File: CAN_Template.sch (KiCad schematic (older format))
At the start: 21 parts, among them U6 SN74LVC1T45DBVR, U7 SN65HVD1050D, U8 MCP2515-xSO, U9 SN74LVC1T45DBVR

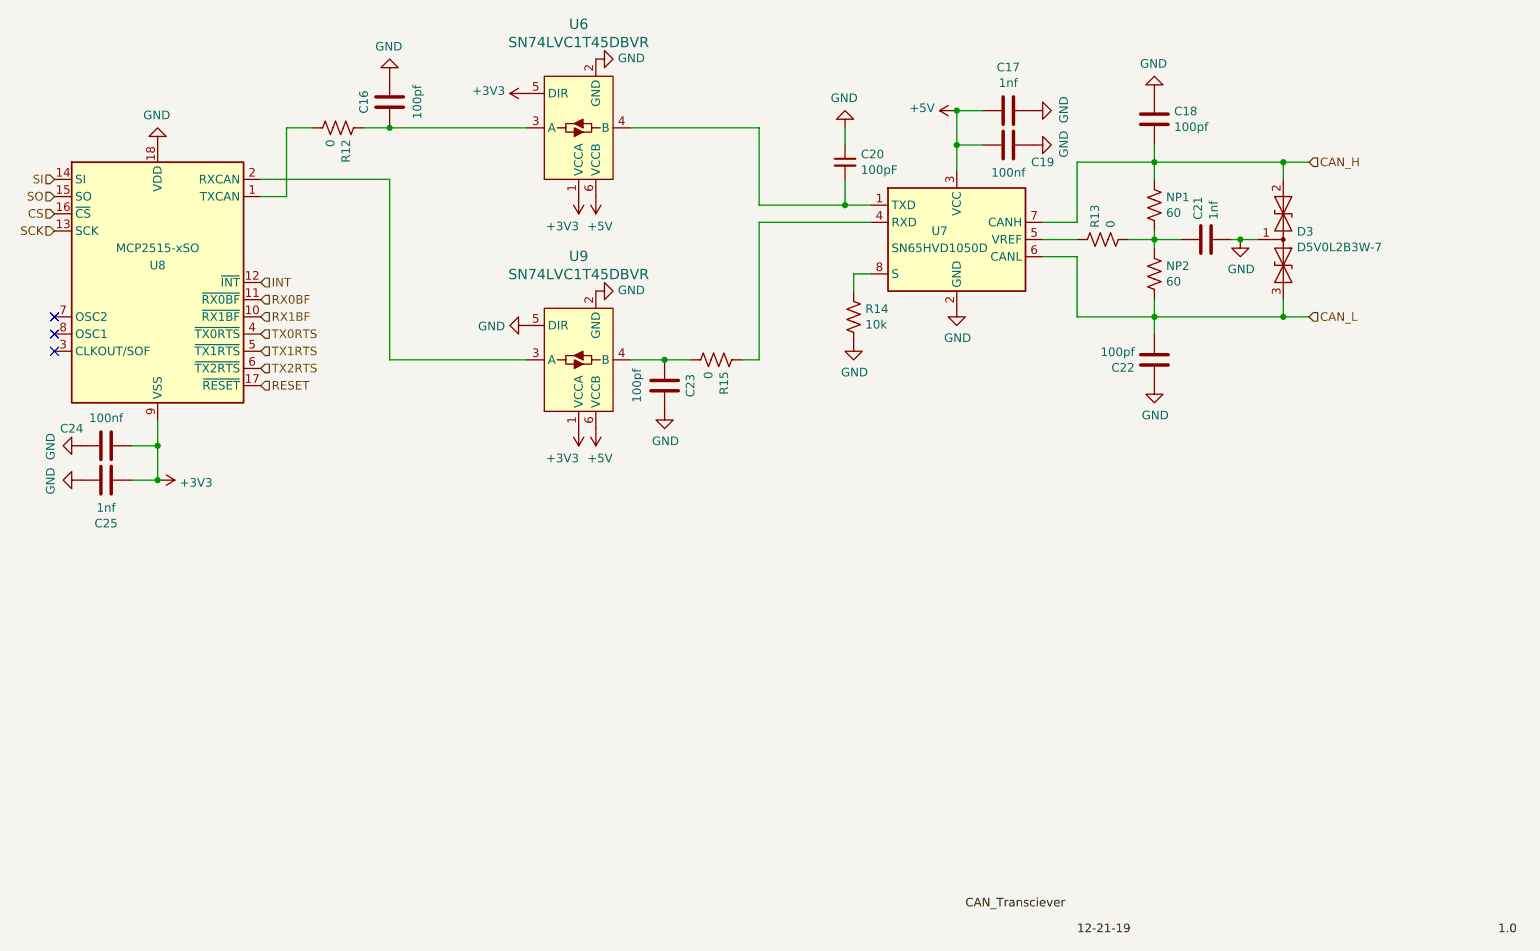
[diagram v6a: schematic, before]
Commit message: Added caps to xbee input, header to SWD pins
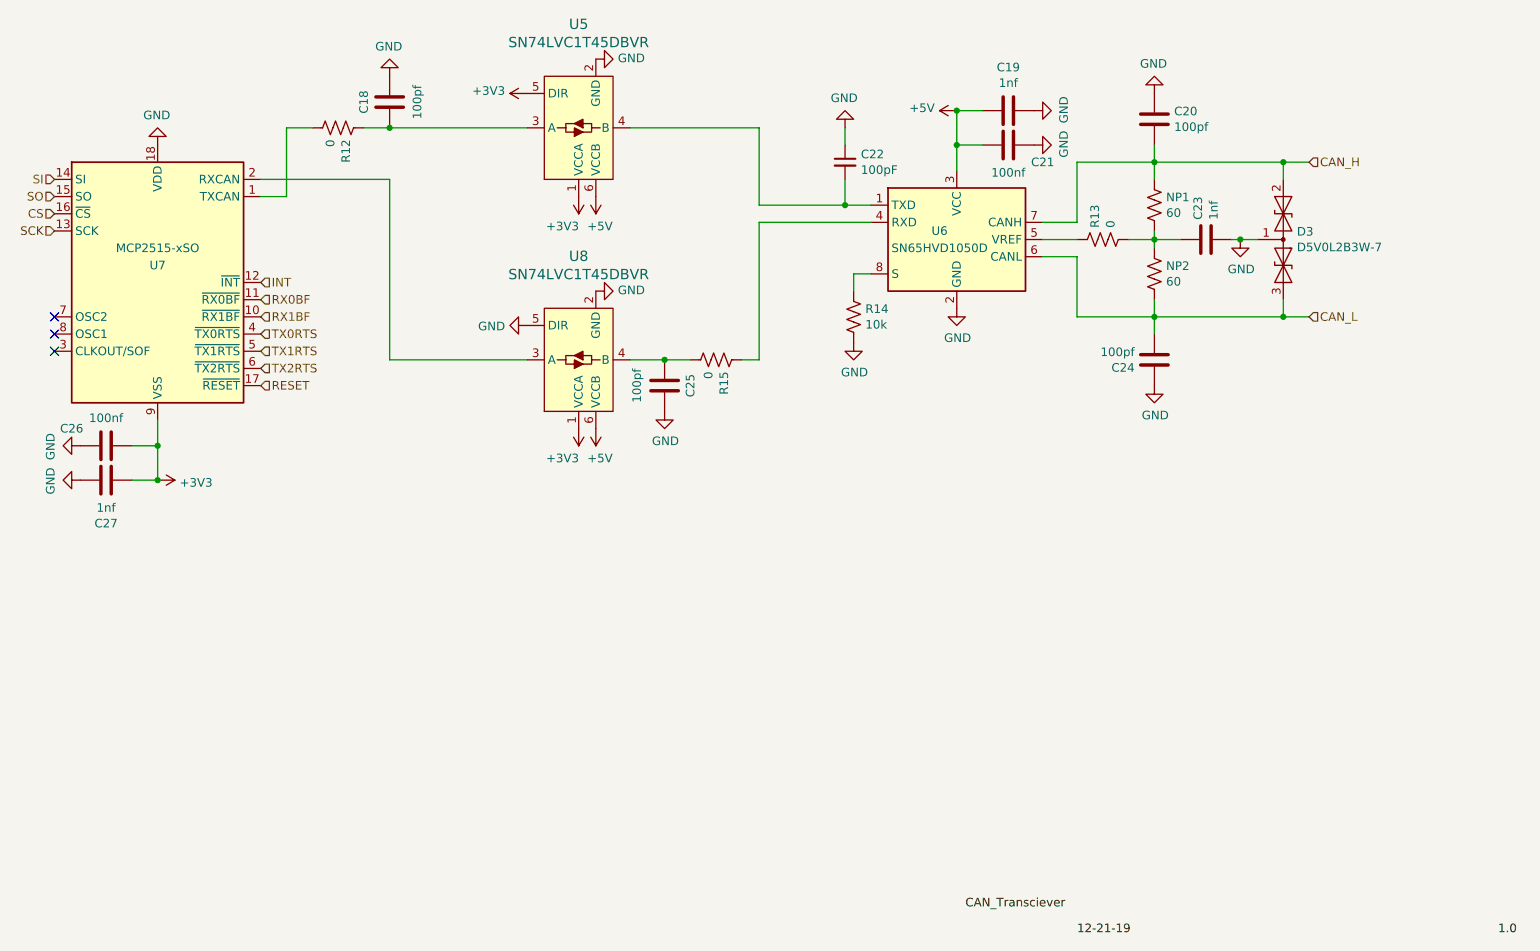
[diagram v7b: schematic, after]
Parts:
- renumbered C16 to C18, C17 to C19, C18 to C20, C19 to C21, C20 to C22, C21 to C23, C22 to C24, C23 to C25, C24 to C26, C25 to C27, U6 to U5, U7 to U6, U8 to U7, U9 to U8
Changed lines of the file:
@@
 $EndComp
 $Comp
-L Device:C C17
+L Device:C C19
 U 1 1 5DCB9CD1
 P 7750 2850
-F 0 "C17" V 7498 2850 50  0000 C CNN
+F 0 "C19" V 7498 2850 50  0000 C CNN
 F 1 "1nf" V 7589 2850 50  0000 C CNN
 F 2 "Capacitor_SMD:C_0805_2012Metric" H 7788 2700 50  0001 C CNN
@@
 $EndComp
 $Comp
-L Device:C C19
+L Device:C C21
 U 1 1 5DCBAD85
 P 7750 3050
-F 0 "C19" V 7650 2850 50  0000 C CNN
+F 0 "C21" V 7650 2850 50  0000 C CNN
 F 1 "100nf" V 7589 3050 50  0000 C CNN
 F 2 "Capacitor_SMD:C_0805_2012Metric" H 7788 2900 50  0001 C CNN
@@
 $EndComp
 $Comp
-L power:GND #PWR055
+L power:GND #PWR057
 U 1 1 5DCE500D
 P 2800 3050
-F 0 "#PWR055" H 2800 2800 50  0001 C CNN
+F 0 "#PWR057" H 2800 2800 50  0001 C CNN
 F 1 "GND" H 2805 2877 50  0000 C CNN
 F 2 "" H 2800 3050 50  0001 C CNN
@@
 $EndComp
 $Comp
-L Device:C C22
+L Device:C C24
 U 1 1 5DCE6703
 P 8600 4300
-F 0 "C22" H 8715 4346 50  0000 L CNN
+F 0 "C24" H 8715 4346 50  0000 L CNN
 F 1 "100pf" H 8715 4255 50  0000 L CNN
 F 2 "Capacitor_SMD:C_0805_2012Metric" H 8638 4150 50  0001 C CNN
@@
 $EndComp
 $Comp
-L Device:C C21
+L Device:C C23
 U 1 1 5DCEFDFD
 P 8900 3600
-F 0 "C21" H 9015 3646 50  0000 L CNN
+F 0 "C23" H 9015 3646 50  0000 L CNN
 F 1 "1nf" H 9015 3555 50  0000 L CNN
 F 2 "Capacitor_SMD:C_0805_2012Metric" H 8938 3450 50  0001 C CNN
@@
 $EndComp
 $Comp
-L power:GND #PWR064
+L power:GND #PWR066
 U 1 1 5DCF0F65
 P 8600 4450
-F 0 "#PWR064" H 8600 4200 50  0001 C CNN
+F 0 "#PWR066" H 8600 4200 50  0001 C CNN
 F 1 "GND" H 8605 4277 50  0000 C CNN
 F 2 "" H 8600 4450 50  0001 C CNN
@@
 $EndComp
 $Comp
-L power:GND #PWR051
+L power:GND #PWR053
 U 1 1 5DCF11EA
 P 8600 2750
-F 0 "#PWR051" H 8600 2500 50  0001 C CNN
+F 0 "#PWR053" H 8600 2500 50  0001 C CNN
 F 1 "GND" H 8605 2577 50  0000 C CNN
 F 2 "" H 8600 2750 50  0001 C CNN
@@
 $EndComp
 $Comp
-L Interface_CAN_LIN:MCP2515-xSO U8
+L Interface_CAN_LIN:MCP2515-xSO U7
 U 1 1 5DCB05B0
 P 2800 3850
-F 0 "U8" H 2800 3950 50  0000 C CNN
+F 0 "U7" H 2800 3950 50  0000 C CNN
 F 1 "MCP2515-xSO" H 2800 4050 50  0000 C CNN
 F 2 "Package_SO:SOIC-18W_7.5x11.6mm_P1.27mm" H 2800 2950 50  0001 C CIN
@@
 CAN_H
 $Comp
-L Device:C C18
+L Device:C C20
 U 1 1 5DCE5998
 P 8600 2900
-F 0 "C18" H 8715 2946 50  0000 L CNN
+F 0 "C20" H 8715 2946 50  0000 L CNN
 F 1 "100pf" H 8715 2855 50  0000 L CNN
 F 2 "Capacitor_SMD:C_0805_2012Metric" H 8638 2750 50  0001 C CNN
@@
 $EndComp
 $Comp
-L Interface_CAN_LIN:SN65HVD1050D U7
+L Interface_CAN_LIN:SN65HVD1050D U6
 U 1 1 5DD4ABBA
 P 7450 3600
-F 0 "U7" H 7350 3650 50  0000 C CNN
+F 0 "U6" H 7350 3650 50  0000 C CNN
 F 1 "SN65HVD1050D" H 7350 3550 50  0000 C CNN
 F 2 "Package_SO:SOIC-8_3.9x4.9mm_P1.27mm" H 7450 3100 50  0001 C CNN
@@
 Connection ~ 9350 3150
 $Comp
-L power:GND #PWR061
+L power:GND #PWR063
 U 1 1 5E09CBC9
 P 7450 4000
-F 0 "#PWR061" H 7450 3750 50  0001 C CNN
+F 0 "#PWR063" H 7450 3750 50  0001 C CNN
 F 1 "GND" H 7455 3827 50  0000 C CNN
 F 2 "" H 7450 4000 50  0001 C CNN
@@
 $EndComp
 $Comp
-L power:GND #PWR056
+L power:GND #PWR058
 U 1 1 5E0A1057
 P 7900 3050
-F 0 "#PWR056" H 7900 2800 50  0001 C CNN
+F 0 "#PWR058" H 7900 2800 50  0001 C CNN
 F 1 "GND" H 7905 2877 50  0000 C CNN
 F 2 "" H 7900 3050 50  0001 C CNN
@@
 $EndComp
 $Comp
-L power:GND #PWR053
+L power:GND #PWR055
 U 1 1 5E0A1679
 P 7900 2850
-F 0 "#PWR053" H 7900 2600 50  0001 C CNN
+F 0 "#PWR055" H 7900 2600 50  0001 C CNN
 F 1 "GND" H 7905 2677 50  0000 C CNN
 F 2 "" H 7900 2850 50  0001 C CNN
@@
 Connection ~ 7450 3050
 $Comp
-L power:+5V #PWR052
+L power:+5V #PWR054
 U 1 1 5E0A2EDD
 P 7450 2850
-F 0 "#PWR052" H 7450 2700 50  0001 C CNN
+F 0 "#PWR054" H 7450 2700 50  0001 C CNN
 F 1 "+5V" V 7465 2978 50  0000 L CNN
 F 2 "" H 7450 2850 50  0001 C CNN
@@
 	6850 3800 6950 3800
 $Comp
-L power:GND #PWR063
+L power:GND #PWR065
 U 1 1 5E0A7026
 P 6850 4200
-F 0 "#PWR063" H 6850 3950 50  0001 C CNN
+F 0 "#PWR065" H 6850 3950 50  0001 C CNN
 F 1 "GND" H 6855 4027 50  0000 C CNN
 F 2 "" H 6850 4200 50  0001 C CNN
@@
 $EndComp
 $Comp
-L Device:C C25
+L Device:C C27
 U 1 1 5E0BDAE5
 P 2500 5000
-F 0 "C25" V 2248 5000 50  0000 C CNN
+F 0 "C27" V 2248 5000 50  0000 C CNN
 F 1 "1nf" V 2339 5000 50  0000 C CNN
 F 2 "Capacitor_SMD:C_0805_2012Metric" H 2538 4850 50  0001 C CNN
@@
 $EndComp
 $Comp
-L Device:C C24
+L Device:C C26
 U 1 1 5E0BDAEB
 P 2500 4800
-F 0 "C24" V 2400 4600 50  0000 C CNN
+F 0 "C26" V 2400 4600 50  0000 C CNN
 F 1 "100nf" V 2339 4800 50  0000 C CNN
 F 2 "Capacitor_SMD:C_0805_2012Metric" H 2538 4650 50  0001 C CNN
@@
 $EndComp
 $Comp
-L power:GND #PWR068
+L power:GND #PWR070
 U 1 1 5E0BDAF1
 P 2350 4800
-F 0 "#PWR068" H 2350 4550 50  0001 C CNN
+F 0 "#PWR070" H 2350 4550 50  0001 C CNN
 F 1 "GND" H 2355 4627 50  0000 C CNN
 F 2 "" H 2350 4800 50  0001 C CNN
@@
 $EndComp
 $Comp
-L power:GND #PWR069
+L power:GND #PWR071
 U 1 1 5E0BDAF7
 P 2350 5000
-F 0 "#PWR069" H 2350 4750 50  0001 C CNN
+F 0 "#PWR071" H 2350 4750 50  0001 C CNN
 F 1 "GND" H 2355 4827 50  0000 C CNN
 F 2 "" H 2350 5000 50  0001 C CNN
@@
 Connection ~ 2800 4800
 $Comp
-L Device:C C16
+L Device:C C18
 U 1 1 5E0C191D
 P 4150 2800
-F 0 "C16" V 4300 2800 50  0000 C CNN
+F 0 "C18" V 4300 2800 50  0000 C CNN
 F 1 "100pf" V 3989 2800 50  0000 C CNN
 F 2 "Capacitor_SMD:C_0805_2012Metric" H 4188 2650 50  0001 C CNN
@@
 	9050 3600 9100 3600
 $Comp
-L power:GND #PWR059
+L power:GND #PWR061
 U 1 1 5E0C862A
 P 9100 3600
-F 0 "#PWR059" H 9100 3350 50  0001 C CNN
+F 0 "#PWR061" H 9100 3350 50  0001 C CNN
 F 1 "GND" H 9105 3427 50  0000 C CNN
 F 2 "" H 9100 3600 50  0001 C CNN
@@
 CAN_Transciever
 $Comp
-L Device:C_Small C20
+L Device:C_Small C22
 U 1 1 5E22EBAC
 P 6800 3150
-F 0 "C20" H 6892 3196 50  0000 L CNN
+F 0 "C22" H 6892 3196 50  0000 L CNN
 F 1 "100pF" H 6892 3105 50  0000 L CNN
 F 2 "Capacitor_SMD:C_0805_2012Metric" H 6800 3150 50  0001 C CNN
@@
 	6800 3400 6800 3250
 $Comp
-L power:GND #PWR054
+L power:GND #PWR056
 U 1 1 5E231658
 P 6800 2950
-F 0 "#PWR054" H 6800 2700 50  0001 C CNN
+F 0 "#PWR056" H 6800 2700 50  0001 C CNN
 F 1 "GND" H 6805 2777 50  0000 C CNN
 F 2 "" H 6800 2950 50  0001 C CNN
@@
 	6800 3050 6800 2950
 $Comp
-L dk_Logic-Translators-Level-Shifters:SN74LVC1T45DBVR U6
+L dk_Logic-Translators-Level-Shifters:SN74LVC1T45DBVR U5
 U 1 1 5E23BA35
 P 5250 2950
-F 0 "U6" H 5250 2347 60  0000 C CNN
+F 0 "U5" H 5250 2347 60  0000 C CNN
 F 1 "SN74LVC1T45DBVR" H 5250 2453 60  0000 C CNN
 F 2 "digikey-footprints:SOT-23-6" H 5450 3150 60  0001 L CNN
@@
 $EndComp
 $Comp
-L dk_Logic-Translators-Level-Shifters:SN74LVC1T45DBVR U9
+L dk_Logic-Translators-Level-Shifters:SN74LVC1T45DBVR U8
 U 1 1 5E2400EF
 P 5250 4300
-F 0 "U9" H 5250 3697 60  0000 C CNN
+F 0 "U8" H 5250 3697 60  0000 C CNN
 F 1 "SN74LVC1T45DBVR" H 5250 3803 60  0000 C CNN
 F 2 "digikey-footprints:SOT-23-6" H 5450 4500 60  0001 L CNN
@@
 	6300 2950 6300 3400
 $Comp
-L power:GND #PWR062
+L power:GND #PWR064
 U 1 1 5E25071C
 P 4950 4100
-F 0 "#PWR062" H 4950 3850 50  0001 C CNN
+F 0 "#PWR064" H 4950 3850 50  0001 C CNN
 F 1 "GND" V 4955 3972 50  0000 R CNN
 F 2 "" H 4950 4100 50  0001 C CNN
@@
 $EndComp
 $Comp
-L power:GND #PWR048
+L power:GND #PWR050
 U 1 1 5E250D83
 P 5350 2550
-F 0 "#PWR048" H 5350 2300 50  0001 C CNN
+F 0 "#PWR050" H 5350 2300 50  0001 C CNN
 F 1 "GND" V 5355 2422 50  0000 R CNN
 F 2 "" H 5350 2550 50  0001 C CNN
@@
 $EndComp
 $Comp
-L power:GND #PWR060
+L power:GND #PWR062
 U 1 1 5E2516EF
 P 5350 3900
-F 0 "#PWR060" H 5350 3650 50  0001 C CNN
+F 0 "#PWR062" H 5350 3650 50  0001 C CNN
 F 1 "GND" V 5355 3772 50  0000 R CNN
 F 2 "" H 5350 3900 50  0001 C CNN
@@
 Connection ~ 6800 3400
 $Comp
-L power:+3V3 #PWR050
+L power:+3V3 #PWR052
 U 1 1 5E2603B1
 P 4950 2750
-F 0 "#PWR050" H 4950 2600 50  0001 C CNN
+F 0 "#PWR052" H 4950 2600 50  0001 C CNN
 F 1 "+3V3" V 4965 2878 50  0000 L CNN
 F 2 "" H 4950 2750 50  0001 C CNN
@@
 	6300 3500 6300 4300
 $Comp
-L power:+3V3 #PWR057
+L power:+3V3 #PWR059
 U 1 1 5E266276
 P 5250 3350
-F 0 "#PWR057" H 5250 3200 50  0001 C CNN
+F 0 "#PWR059" H 5250 3200 50  0001 C CNN
 F 1 "+3V3" H 5344 3523 50  0000 C CNN
 F 2 "" H 5250 3350 50  0001 C CNN
@@
 $EndComp
 $Comp
-L power:+5V #PWR058
+L power:+5V #PWR060
 U 1 1 5E2667FA
 P 5350 3350
-F 0 "#PWR058" H 5350 3200 50  0001 C CNN
+F 0 "#PWR060" H 5350 3200 50  0001 C CNN
 F 1 "+5V" H 5326 3523 50  0000 C CNN
 F 2 "" H 5350 3350 50  0001 C CNN
@@
 $EndComp
 $Comp
-L power:+3V3 #PWR066
+L power:+3V3 #PWR068
 U 1 1 5E267CF5
 P 5250 4700
-F 0 "#PWR066" H 5250 4550 50  0001 C CNN
+F 0 "#PWR068" H 5250 4550 50  0001 C CNN
 F 1 "+3V3" H 5344 4873 50  0000 C CNN
 F 2 "" H 5250 4700 50  0001 C CNN
@@
 $EndComp
 $Comp
-L power:+5V #PWR067
+L power:+5V #PWR069
 U 1 1 5E267CFB
 P 5350 4700
-F 0 "#PWR067" H 5350 4550 50  0001 C CNN
+F 0 "#PWR069" H 5350 4550 50  0001 C CNN
 F 1 "+5V" H 5326 4873 50  0000 C CNN
 F 2 "" H 5350 4700 50  0001 C CNN
@@
 $EndComp
 $Comp
-L power:+3V3 #PWR070
+L power:+3V3 #PWR072
 U 1 1 5E269EEC
 P 2800 5000
-F 0 "#PWR070" H 2800 4850 50  0001 C CNN
+F 0 "#PWR072" H 2800 4850 50  0001 C CNN
 F 1 "+3V3" V 2815 5128 50  0000 L CNN
 F 2 "" H 2800 5000 50  0001 C CNN
@@
 Connection ~ 4150 2950
 $Comp
-L power:GND #PWR049
+L power:GND #PWR051
 U 1 1 5E0C3AF0
 P 4150 2650
-F 0 "#PWR049" H 4150 2400 50  0001 C CNN
+F 0 "#PWR051" H 4150 2400 50  0001 C CNN
 F 1 "GND" H 4155 2477 50  0000 C CNN
 F 2 "" H 4150 2650 50  0001 C CNN
@@
 	4000 2950 4150 2950
 $Comp
-L Device:C C23
+L Device:C C25
 U 1 1 5E289934
 P 5750 4450
-F 0 "C23" V 5900 4450 50  0000 C CNN
+F 0 "C25" V 5900 4450 50  0000 C CNN
 F 1 "100pf" V 5589 4450 50  0000 C CNN
 F 2 "Capacitor_SMD:C_0805_2012Metric" H 5788 4300 50  0001 C CNN
@@
 $EndComp
 $Comp
-L power:GND #PWR065
+L power:GND #PWR067
 U 1 1 5E28993A
 P 5750 4600
-F 0 "#PWR065" H 5750 4350 50  0001 C CNN
+F 0 "#PWR067" H 5750 4350 50  0001 C CNN
 F 1 "GND" H 5755 4427 50  0000 C CNN
 F 2 "" H 5750 4600 50  0001 C CNN

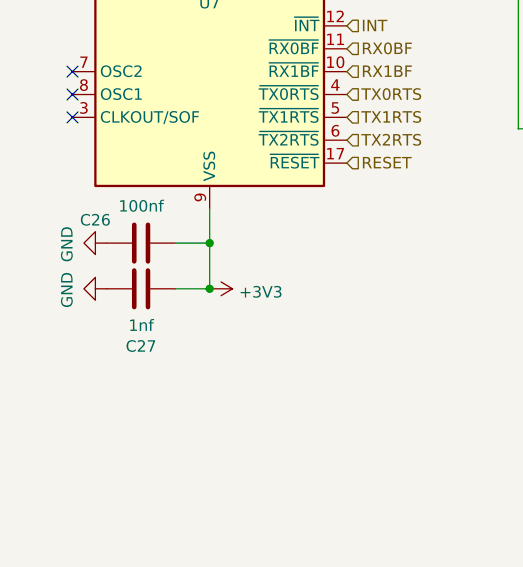
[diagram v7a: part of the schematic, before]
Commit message: added solder bridges, placed a few components on board
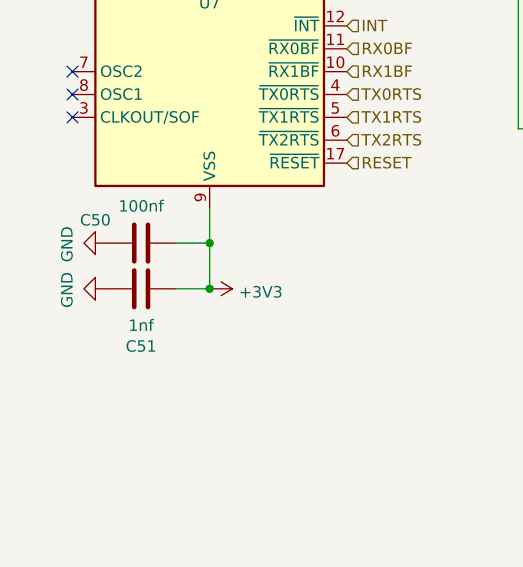
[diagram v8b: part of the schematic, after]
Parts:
- renumbered C26 to C50, C27 to C51
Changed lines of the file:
@@
 $EndComp
 $Comp
-L Device:C C27
+L Device:C C51
 U 1 1 5E0BDAE5
 P 2500 5000
-F 0 "C27" V 2248 5000 50  0000 C CNN
+F 0 "C51" V 2248 5000 50  0000 C CNN
 F 1 "1nf" V 2339 5000 50  0000 C CNN
 F 2 "Capacitor_SMD:C_0805_2012Metric" H 2538 4850 50  0001 C CNN
@@
 $EndComp
 $Comp
-L Device:C C26
+L Device:C C50
 U 1 1 5E0BDAEB
 P 2500 4800
-F 0 "C26" V 2400 4600 50  0000 C CNN
+F 0 "C50" V 2400 4600 50  0000 C CNN
 F 1 "100nf" V 2339 4800 50  0000 C CNN
 F 2 "Capacitor_SMD:C_0805_2012Metric" H 2538 4650 50  0001 C CNN
@@
 $EndComp
 $Comp
-L power:+3V3 #PWR068
-U 1 1 5E267CF5
-P 5250 4700
-F 0 "#PWR068" H 5250 4550 50  0001 C CNN
-F 1 "+3V3" H 5344 4873 50  0000 C CNN
-F 2 "" H 5250 4700 50  0001 C CNN
-F 3 "" H 5250 4700 50  0001 C CNN
-	1    5250 4700
-	-1   0    0    1
-$EndComp
-$Comp
-L power:+5V #PWR069
-U 1 1 5E267CFB
-P 5350 4700
-F 0 "#PWR069" H 5350 4550 50  0001 C CNN
-F 1 "+5V" H 5326 4873 50  0000 C CNN
-F 2 "" H 5350 4700 50  0001 C CNN
-F 3 "" H 5350 4700 50  0001 C CNN
-	1    5350 4700
-	-1   0    0    1
-$EndComp
-$Comp
 L power:+3V3 #PWR072
 U 1 1 5E269EEC
@@
 	6200 4300 6300 4300
 Connection ~ 5750 4300
+$Comp
+L power:+5V #PWR069
+U 1 1 5E267CFB
+P 5350 4700
+F 0 "#PWR069" H 5350 4550 50  0001 C CNN
+F 1 "+5V" H 5326 4873 50  0000 C CNN
+F 2 "" H 5350 4700 50  0001 C CNN
+F 3 "" H 5350 4700 50  0001 C CNN
+	1    5350 4700
+	-1   0    0    1
+$EndComp
+$Comp
+L power:+3V3 #PWR068
+U 1 1 5E267CF5
+P 5250 4700
+F 0 "#PWR068" H 5250 4550 50  0001 C CNN
+F 1 "+3V3" H 5344 4873 50  0000 C CNN
+F 2 "" H 5250 4700 50  0001 C CNN
+F 3 "" H 5250 4700 50  0001 C CNN
+	1    5250 4700
+	-1   0    0    1
+$EndComp
 $EndSCHEMATC
